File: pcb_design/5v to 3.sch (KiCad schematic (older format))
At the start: 6 parts

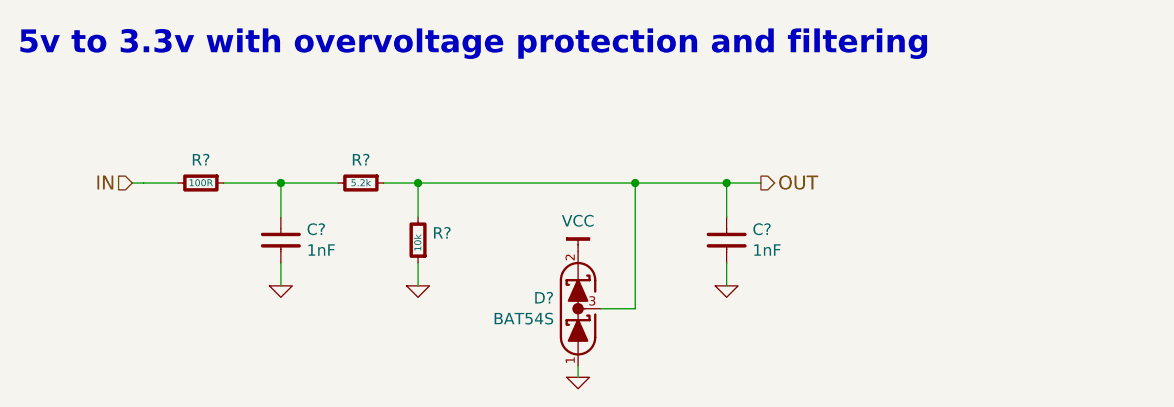
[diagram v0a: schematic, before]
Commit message: Components placement, 3D models, updated some footprints to nominal IPC type
Signed-off-by: Marcos Chaparro <mchaparro@paltatech.com>
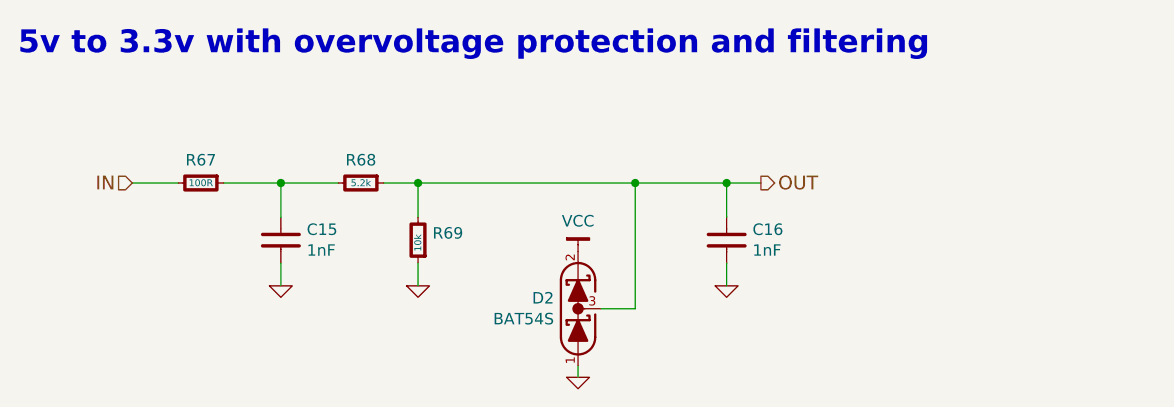
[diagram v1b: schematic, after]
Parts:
- gave numbers to parts that had none: 6
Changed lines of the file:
@@
 $Descr A4 11693 8268
 encoding utf-8
-Sheet 12 12
+Sheet 11 12
 Title ""
 Date ""
@@
 OUT
 $Comp
-L BAT54S D?
+L BAT54S D1
 U 1 1 5889F39B
 P 5950 4300
-AR Path="/5889B2E2/5889F39B" Ref="D?"  Part="1"
-AR Path="/5889CDF9/5889F39B" Ref="D?"  Part="1"
-F 0 "D?" V 5996 4195 50  0000 R CNN
+AR Path="/5889B2E2/5889F39B" Ref="D1"  Part="1"
+AR Path="/5889CDF9/5889F39B" Ref="D2"  Part="1"
+F 0 "D2" V 5996 4195 50  0000 R CNN
 F 1 "BAT54S" V 5905 4195 50  0000 R CNN
 F 2 "smd-semi:SOT-23" H 5950 4150 60  0001 C CNN
@@
 $EndComp
 $Comp
-L GND #PWR?
+L GND #PWR91
 U 1 1 5889F466
 P 5950 4600
-AR Path="/5889B2E2/5889F466" Ref="#PWR?"  Part="1"
-AR Path="/5889CDF9/5889F466" Ref="#PWR?"  Part="1"
-F 0 "#PWR?" H 5950 4600 30  0001 C CNN
+AR Path="/5889B2E2/5889F466" Ref="#PWR91"  Part="1"
+AR Path="/5889CDF9/5889F466" Ref="#PWR96"  Part="1"
+F 0 "#PWR96" H 5950 4600 30  0001 C CNN
 F 1 "GND" H 5950 4530 30  0001 C CNN
 F 2 "" H 5950 4600 60  0000 C CNN
@@
 $EndComp
 $Comp
-L R-0603 R?
+L R-0603 R64
 U 1 1 5889F74D
 P 4300 3750
-AR Path="/5889B2E2/5889F74D" Ref="R?"  Part="1"
-AR Path="/5889CDF9/5889F74D" Ref="R?"  Part="1"
-F 0 "R?" V 4200 3750 50  0000 C CNN
+AR Path="/5889B2E2/5889F74D" Ref="R64"  Part="1"
+AR Path="/5889CDF9/5889F74D" Ref="R67"  Part="1"
+F 0 "R67" V 4200 3750 50  0000 C CNN
 F 1 "100R" V 4300 3750 30  0000 C CNN
 F 2 "IPC7351-Nominal:RESC1608X50" H 4300 3750 50  0001 C CNN
@@
 $EndComp
 $Comp
-L R-0603 R?
+L R-0603 R65
 U 1 1 5889F796
 P 5000 3750
-AR Path="/5889B2E2/5889F796" Ref="R?"  Part="1"
-AR Path="/5889CDF9/5889F796" Ref="R?"  Part="1"
-F 0 "R?" V 4900 3750 50  0000 C CNN
+AR Path="/5889B2E2/5889F796" Ref="R65"  Part="1"
+AR Path="/5889CDF9/5889F796" Ref="R68"  Part="1"
+F 0 "R68" V 4900 3750 50  0000 C CNN
 F 1 "5.2k" V 5000 3750 30  0000 C CNN
 F 2 "IPC7351-Nominal:RESC1608X50" H 5000 3750 50  0001 C CNN
@@
 $EndComp
 $Comp
-L R-0603 R?
+L R-0603 R66
 U 1 1 5889F7E7
 P 5250 4000
-AR Path="/5889B2E2/5889F7E7" Ref="R?"  Part="1"
-AR Path="/5889CDF9/5889F7E7" Ref="R?"  Part="1"
-F 0 "R?" H 5187 3970 50  0000 R CNN
+AR Path="/5889B2E2/5889F7E7" Ref="R66"  Part="1"
+AR Path="/5889CDF9/5889F7E7" Ref="R69"  Part="1"
+F 0 "R69" H 5187 3970 50  0000 R CNN
 F 1 "10k" V 5250 4050 30  0000 R CNN
 F 2 "IPC7351-Nominal:RESC1608X50" H 5250 4000 50  0001 C CNN
@@
 $EndComp
 $Comp
-L C-0603 C?
+L C-0603 C13
 U 1 1 5889F81D
 P 4650 4000
-AR Path="/5889B2E2/5889F81D" Ref="C?"  Part="1"
-AR Path="/5889CDF9/5889F81D" Ref="C?"  Part="1"
-F 0 "C?" H 4763 4046 50  0000 L CNN
+AR Path="/5889B2E2/5889F81D" Ref="C13"  Part="1"
+AR Path="/5889CDF9/5889F81D" Ref="C15"  Part="1"
+F 0 "C15" H 4763 4046 50  0000 L CNN
 F 1 "1nF" H 4763 3955 50  0000 L CNN
 F 2 "IPC7351-Nominal:CAPC1608X55" H 4650 4000 50  0001 C CNN
@@
 $EndComp
 $Comp
-L GND #PWR?
+L GND #PWR89
 U 1 1 5889F89D
 P 5250 4200
-AR Path="/5889B2E2/5889F89D" Ref="#PWR?"  Part="1"
-AR Path="/5889CDF9/5889F89D" Ref="#PWR?"  Part="1"
-F 0 "#PWR?" H 5250 4200 30  0001 C CNN
+AR Path="/5889B2E2/5889F89D" Ref="#PWR89"  Part="1"
+AR Path="/5889CDF9/5889F89D" Ref="#PWR94"  Part="1"
+F 0 "#PWR94" H 5250 4200 30  0001 C CNN
 F 1 "GND" H 5250 4130 30  0001 C CNN
 F 2 "" H 5250 4200 60  0000 C CNN
@@
 $EndComp
 $Comp
-L GND #PWR?
+L GND #PWR88
 U 1 1 5889F8B7
 P 4650 4200
-AR Path="/5889B2E2/5889F8B7" Ref="#PWR?"  Part="1"
-AR Path="/5889CDF9/5889F8B7" Ref="#PWR?"  Part="1"
-F 0 "#PWR?" H 4650 4200 30  0001 C CNN
+AR Path="/5889B2E2/5889F8B7" Ref="#PWR88"  Part="1"
+AR Path="/5889CDF9/5889F8B7" Ref="#PWR93"  Part="1"
+F 0 "#PWR93" H 4650 4200 30  0001 C CNN
 F 1 "GND" H 4650 4130 30  0001 C CNN
 F 2 "" H 4650 4200 60  0000 C CNN
@@
 $EndComp
 $Comp
-L VCC #PWR?
+L VCC #PWR90
 U 1 1 5889F92D
 P 5950 4050
-AR Path="/5889B2E2/5889F92D" Ref="#PWR?"  Part="1"
-AR Path="/5889CDF9/5889F92D" Ref="#PWR?"  Part="1"
-F 0 "#PWR?" H 5950 4100 30  0001 C CNN
+AR Path="/5889B2E2/5889F92D" Ref="#PWR90"  Part="1"
+AR Path="/5889CDF9/5889F92D" Ref="#PWR95"  Part="1"
+F 0 "#PWR95" H 5950 4100 30  0001 C CNN
 F 1 "VCC" H 5950 4183 50  0000 C CNN
 F 2 "" H 5950 4050 60  0000 C CNN
@@
 $EndComp
 $Comp
-L C-0603 C?
+L C-0603 C14
 U 1 1 5889FB1A
 P 6600 4000
-AR Path="/5889B2E2/5889FB1A" Ref="C?"  Part="1"
-AR Path="/5889CDF9/5889FB1A" Ref="C?"  Part="1"
-F 0 "C?" H 6713 4046 50  0000 L CNN
+AR Path="/5889B2E2/5889FB1A" Ref="C14"  Part="1"
+AR Path="/5889CDF9/5889FB1A" Ref="C16"  Part="1"
+F 0 "C16" H 6713 4046 50  0000 L CNN
 F 1 "1nF" H 6713 3955 50  0000 L CNN
 F 2 "IPC7351-Nominal:CAPC1608X55" H 6600 4000 50  0001 C CNN
@@
 $EndComp
 $Comp
-L GND #PWR?
+L GND #PWR92
 U 1 1 5889FBDC
 P 6600 4200
-AR Path="/5889B2E2/5889FBDC" Ref="#PWR?"  Part="1"
-AR Path="/5889CDF9/5889FBDC" Ref="#PWR?"  Part="1"
-F 0 "#PWR?" H 6600 4200 30  0001 C CNN
+AR Path="/5889B2E2/5889FBDC" Ref="#PWR92"  Part="1"
+AR Path="/5889CDF9/5889FBDC" Ref="#PWR97"  Part="1"
+F 0 "#PWR97" H 6600 4200 30  0001 C CNN
 F 1 "GND" H 6600 4130 30  0001 C CNN
 F 2 "" H 6600 4200 60  0000 C CNN
@@
 	6200 4300 6200 3750
 Wire Wire Line
-	5100 3750 5250 3750
-Wire Wire Line
-	5250 3750 6200 3750
-Wire Wire Line
-	6200 3750 6600 3750
-Wire Wire Line
-	6600 3750 6750 3750
+	5100 3750 6750 3750
 Wire Wire Line
 	5950 4550 5950 4600
 Wire Wire Line
-	4200 3750 4050 3750
-Wire Wire Line
-	4050 3750 4000 3750
+	4000 3750 4200 3750
 Wire Wire Line
 	4650 3900 4650 3750
 Wire Wire Line
-	4400 3750 4650 3750
-Wire Wire Line
-	4650 3750 4900 3750
+	4400 3750 4900 3750
 Connection ~ 4650 3750
 Wire Wire Line

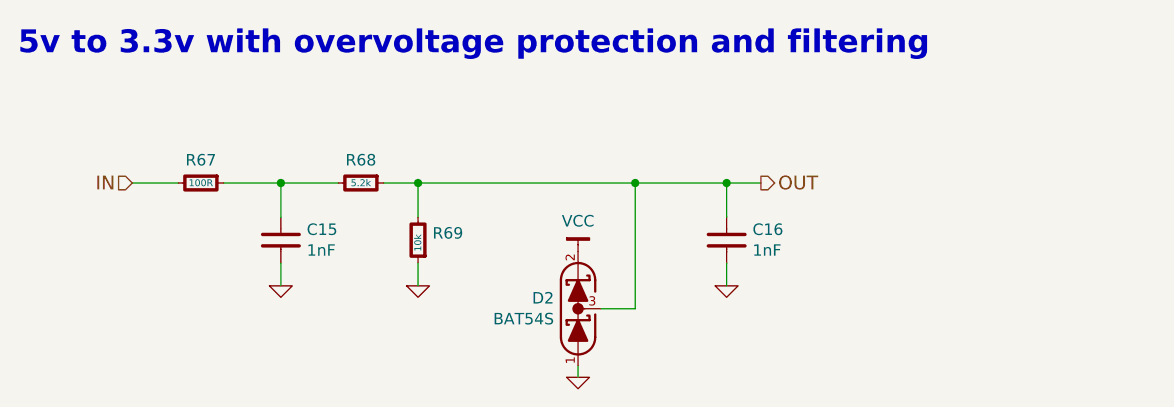
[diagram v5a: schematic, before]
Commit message: More layout. Changed LED pin. Added placeholder for a resolver IC
Signed-off-by: Marcos Chaparro <mchaparro@paltatech.com>
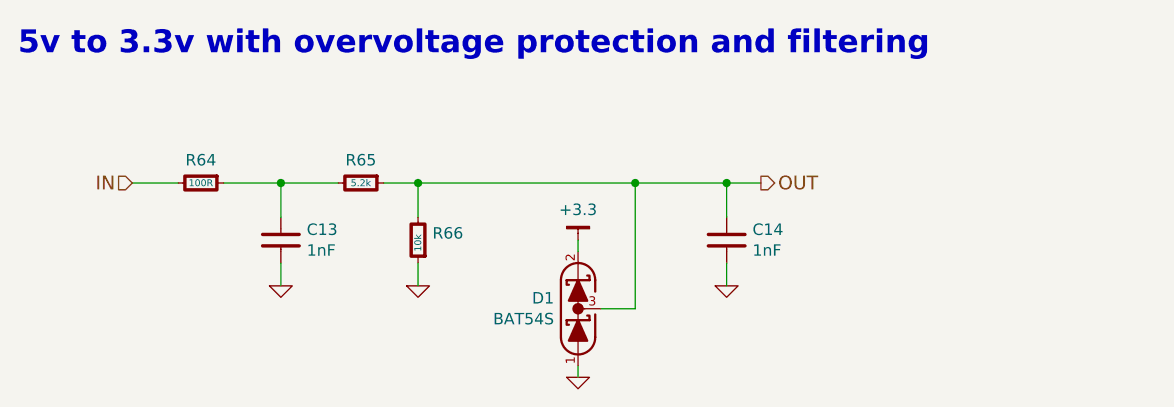
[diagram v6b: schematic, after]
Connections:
- net VCC renamed +3.3
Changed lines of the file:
@@
 $Descr A4 11693 8268
 encoding utf-8
-Sheet 11 13
+Sheet 11 14
 Title "5v to 3.3v conditioning"
 Date "2017-01-24"
@@
 AR Path="/5889B2E2/5889F39B" Ref="D1"  Part="1"
 AR Path="/5889CDF9/5889F39B" Ref="D2"  Part="1"
-F 0 "D2" V 5996 4195 50  0000 R CNN
+F 0 "D1" V 5996 4195 50  0000 R CNN
 F 1 "BAT54S" V 5905 4195 50  0000 R CNN
 F 2 "smd-semi:SOT-23" H 5950 4150 60  0001 C CNN
@@
 $EndComp
 $Comp
-L GND #PWR138
+L GND #PWR0135
 U 1 1 5889F466
 P 5950 4600
-AR Path="/5889B2E2/5889F466" Ref="#PWR138"  Part="1"
-AR Path="/5889CDF9/5889F466" Ref="#PWR143"  Part="1"
-F 0 "#PWR143" H 5950 4600 30  0001 C CNN
+AR Path="/5889B2E2/5889F466" Ref="#PWR0135"  Part="1"
+AR Path="/5889CDF9/5889F466" Ref="#PWR0140"  Part="1"
+F 0 "#PWR0135" H 5950 4600 30  0001 C CNN
 F 1 "GND" H 5950 4530 30  0001 C CNN
 F 2 "" H 5950 4600 60  0000 C CNN
@@
 AR Path="/5889B2E2/5889F74D" Ref="R64"  Part="1"
 AR Path="/5889CDF9/5889F74D" Ref="R67"  Part="1"
-F 0 "R67" V 4200 3750 50  0000 C CNN
+F 0 "R64" V 4200 3750 50  0000 C CNN
 F 1 "100R" V 4300 3750 30  0000 C CNN
 F 2 "IPC7351-Nominal:RESC1608X50" H 4300 3750 50  0001 C CNN
@@
 AR Path="/5889B2E2/5889F796" Ref="R65"  Part="1"
 AR Path="/5889CDF9/5889F796" Ref="R68"  Part="1"
-F 0 "R68" V 4900 3750 50  0000 C CNN
+F 0 "R65" V 4900 3750 50  0000 C CNN
 F 1 "5.2k" V 5000 3750 30  0000 C CNN
 F 2 "IPC7351-Nominal:RESC1608X50" H 5000 3750 50  0001 C CNN
@@
 AR Path="/5889B2E2/5889F7E7" Ref="R66"  Part="1"
 AR Path="/5889CDF9/5889F7E7" Ref="R69"  Part="1"
-F 0 "R69" H 5187 3970 50  0000 R CNN
+F 0 "R66" H 5187 3970 50  0000 R CNN
 F 1 "10k" V 5250 4050 30  0000 R CNN
 F 2 "IPC7351-Nominal:RESC1608X50" H 5250 4000 50  0001 C CNN
@@
 AR Path="/5889B2E2/5889F81D" Ref="C13"  Part="1"
 AR Path="/5889CDF9/5889F81D" Ref="C15"  Part="1"
-F 0 "C15" H 4763 4046 50  0000 L CNN
+F 0 "C13" H 4763 4046 50  0000 L CNN
 F 1 "1nF" H 4763 3955 50  0000 L CNN
 F 2 "IPC7351-Nominal:CAPC1608X55" H 4650 4000 50  0001 C CNN
@@
 $EndComp
 $Comp
-L GND #PWR136
+L GND #PWR0136
 U 1 1 5889F89D
 P 5250 4200
-AR Path="/5889B2E2/5889F89D" Ref="#PWR136"  Part="1"
-AR Path="/5889CDF9/5889F89D" Ref="#PWR141"  Part="1"
-F 0 "#PWR141" H 5250 4200 30  0001 C CNN
+AR Path="/5889B2E2/5889F89D" Ref="#PWR0136"  Part="1"
+AR Path="/5889CDF9/5889F89D" Ref="#PWR0141"  Part="1"
+F 0 "#PWR0136" H 5250 4200 30  0001 C CNN
 F 1 "GND" H 5250 4130 30  0001 C CNN
 F 2 "" H 5250 4200 60  0000 C CNN
@@
 $EndComp
 $Comp
-L GND #PWR135
+L GND #PWR0137
 U 1 1 5889F8B7
 P 4650 4200
-AR Path="/5889B2E2/5889F8B7" Ref="#PWR135"  Part="1"
-AR Path="/5889CDF9/5889F8B7" Ref="#PWR140"  Part="1"
-F 0 "#PWR140" H 4650 4200 30  0001 C CNN
+AR Path="/5889B2E2/5889F8B7" Ref="#PWR0137"  Part="1"
+AR Path="/5889CDF9/5889F8B7" Ref="#PWR0142"  Part="1"
+F 0 "#PWR0137" H 4650 4200 30  0001 C CNN
 F 1 "GND" H 4650 4130 30  0001 C CNN
 F 2 "" H 4650 4200 60  0000 C CNN
 F 3 "" H 4650 4200 60  0000 C CNN
 	1    4650 4200
-	1    0    0    -1
-$EndComp
-$Comp
-L VCC #PWR137
-U 1 1 5889F92D
-P 5950 4050
-AR Path="/5889B2E2/5889F92D" Ref="#PWR137"  Part="1"
-AR Path="/5889CDF9/5889F92D" Ref="#PWR142"  Part="1"
-F 0 "#PWR142" H 5950 4100 30  0001 C CNN
-F 1 "VCC" H 5950 4183 50  0000 C CNN
-F 2 "" H 5950 4050 60  0000 C CNN
-F 3 "" H 5950 4050 60  0000 C CNN
-	1    5950 4050
 	1    0    0    -1
 $EndComp
@@
 AR Path="/5889B2E2/5889FB1A" Ref="C14"  Part="1"
 AR Path="/5889CDF9/5889FB1A" Ref="C16"  Part="1"
-F 0 "C16" H 6713 4046 50  0000 L CNN
+F 0 "C14" H 6713 4046 50  0000 L CNN
 F 1 "1nF" H 6713 3955 50  0000 L CNN
 F 2 "IPC7351-Nominal:CAPC1608X55" H 6600 4000 50  0001 C CNN
@@
 $EndComp
 $Comp
-L GND #PWR139
+L GND #PWR0139
 U 1 1 5889FBDC
 P 6600 4200
-AR Path="/5889B2E2/5889FBDC" Ref="#PWR139"  Part="1"
-AR Path="/5889CDF9/5889FBDC" Ref="#PWR144"  Part="1"
-F 0 "#PWR144" H 6600 4200 30  0001 C CNN
+AR Path="/5889B2E2/5889FBDC" Ref="#PWR0139"  Part="1"
+AR Path="/5889CDF9/5889FBDC" Ref="#PWR0144"  Part="1"
+F 0 "#PWR0139" H 6600 4200 30  0001 C CNN
 F 1 "GND" H 6600 4130 30  0001 C CNN
 F 2 "" H 6600 4200 60  0000 C CNN
@@
 Text Notes 3500 3200 0    100  ~ 20
 5v to 3.3v with overvoltage protection and filtering
+$Comp
+L +3.3 #PWR?
+U 1 1 588FFFB4
+P 5950 4000
+F 0 "#PWR?" H 0   50  30  0001 C CNN
+F 1 "+3.3" H 5950 4133 50  0000 C CNN
+F 2 "" H 0   0   60  0000 C CNN
+F 3 "" H 0   0   60  0000 C CNN
+	1    5950 4000
+	1    0    0    -1
+$EndComp
+Wire Wire Line
+	5950 4000 5950 4050
 $EndSCHEMATC

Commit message: Added reverse polarity protection on the isolated side of CON connector. Also, more layout
Signed-off-by: Marcos Chaparro <mchaparro@paltatech.com>
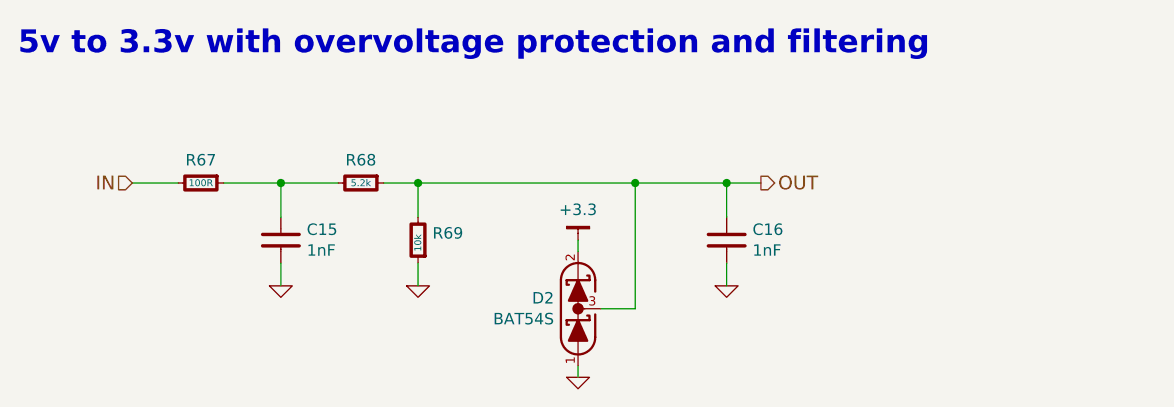
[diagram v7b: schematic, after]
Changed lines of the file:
@@
 AR Path="/5889B2E2/5889F39B" Ref="D1"  Part="1"
 AR Path="/5889CDF9/5889F39B" Ref="D2"  Part="1"
-F 0 "D1" V 5996 4195 50  0000 R CNN
+F 0 "D2" V 5996 4195 50  0000 R CNN
 F 1 "BAT54S" V 5905 4195 50  0000 R CNN
 F 2 "smd-semi:SOT-23" H 5950 4150 60  0001 C CNN
@@
 $EndComp
 $Comp
-L GND #PWR0135
+L GND #PWR142
 U 1 1 5889F466
 P 5950 4600
-AR Path="/5889B2E2/5889F466" Ref="#PWR0135"  Part="1"
-AR Path="/5889CDF9/5889F466" Ref="#PWR0140"  Part="1"
-F 0 "#PWR0135" H 5950 4600 30  0001 C CNN
+AR Path="/5889B2E2/5889F466" Ref="#PWR142"  Part="1"
+AR Path="/5889CDF9/5889F466" Ref="#PWR147"  Part="1"
+F 0 "#PWR147" H 5950 4600 30  0001 C CNN
 F 1 "GND" H 5950 4530 30  0001 C CNN
 F 2 "" H 5950 4600 60  0000 C CNN
@@
 AR Path="/5889B2E2/5889F74D" Ref="R64"  Part="1"
 AR Path="/5889CDF9/5889F74D" Ref="R67"  Part="1"
-F 0 "R64" V 4200 3750 50  0000 C CNN
+F 0 "R67" V 4200 3750 50  0000 C CNN
 F 1 "100R" V 4300 3750 30  0000 C CNN
 F 2 "IPC7351-Nominal:RESC1608X50" H 4300 3750 50  0001 C CNN
@@
 AR Path="/5889B2E2/5889F796" Ref="R65"  Part="1"
 AR Path="/5889CDF9/5889F796" Ref="R68"  Part="1"
-F 0 "R65" V 4900 3750 50  0000 C CNN
+F 0 "R68" V 4900 3750 50  0000 C CNN
 F 1 "5.2k" V 5000 3750 30  0000 C CNN
 F 2 "IPC7351-Nominal:RESC1608X50" H 5000 3750 50  0001 C CNN
@@
 AR Path="/5889B2E2/5889F7E7" Ref="R66"  Part="1"
 AR Path="/5889CDF9/5889F7E7" Ref="R69"  Part="1"
-F 0 "R66" H 5187 3970 50  0000 R CNN
+F 0 "R69" H 5187 3970 50  0000 R CNN
 F 1 "10k" V 5250 4050 30  0000 R CNN
 F 2 "IPC7351-Nominal:RESC1608X50" H 5250 4000 50  0001 C CNN
@@
 AR Path="/5889B2E2/5889F81D" Ref="C13"  Part="1"
 AR Path="/5889CDF9/5889F81D" Ref="C15"  Part="1"
-F 0 "C13" H 4763 4046 50  0000 L CNN
+F 0 "C15" H 4763 4046 50  0000 L CNN
 F 1 "1nF" H 4763 3955 50  0000 L CNN
 F 2 "IPC7351-Nominal:CAPC1608X55" H 4650 4000 50  0001 C CNN
@@
 $EndComp
 $Comp
-L GND #PWR0136
+L GND #PWR140
 U 1 1 5889F89D
 P 5250 4200
-AR Path="/5889B2E2/5889F89D" Ref="#PWR0136"  Part="1"
-AR Path="/5889CDF9/5889F89D" Ref="#PWR0141"  Part="1"
-F 0 "#PWR0136" H 5250 4200 30  0001 C CNN
+AR Path="/5889B2E2/5889F89D" Ref="#PWR140"  Part="1"
+AR Path="/5889CDF9/5889F89D" Ref="#PWR145"  Part="1"
+F 0 "#PWR145" H 5250 4200 30  0001 C CNN
 F 1 "GND" H 5250 4130 30  0001 C CNN
 F 2 "" H 5250 4200 60  0000 C CNN
@@
 $EndComp
 $Comp
-L GND #PWR0137
+L GND #PWR139
 U 1 1 5889F8B7
 P 4650 4200
-AR Path="/5889B2E2/5889F8B7" Ref="#PWR0137"  Part="1"
-AR Path="/5889CDF9/5889F8B7" Ref="#PWR0142"  Part="1"
-F 0 "#PWR0137" H 4650 4200 30  0001 C CNN
+AR Path="/5889B2E2/5889F8B7" Ref="#PWR139"  Part="1"
+AR Path="/5889CDF9/5889F8B7" Ref="#PWR144"  Part="1"
+F 0 "#PWR144" H 4650 4200 30  0001 C CNN
 F 1 "GND" H 4650 4130 30  0001 C CNN
 F 2 "" H 4650 4200 60  0000 C CNN
@@
 AR Path="/5889B2E2/5889FB1A" Ref="C14"  Part="1"
 AR Path="/5889CDF9/5889FB1A" Ref="C16"  Part="1"
-F 0 "C14" H 6713 4046 50  0000 L CNN
+F 0 "C16" H 6713 4046 50  0000 L CNN
 F 1 "1nF" H 6713 3955 50  0000 L CNN
 F 2 "IPC7351-Nominal:CAPC1608X55" H 6600 4000 50  0001 C CNN
@@
 $EndComp
 $Comp
-L GND #PWR0139
+L GND #PWR143
 U 1 1 5889FBDC
 P 6600 4200
-AR Path="/5889B2E2/5889FBDC" Ref="#PWR0139"  Part="1"
-AR Path="/5889CDF9/5889FBDC" Ref="#PWR0144"  Part="1"
-F 0 "#PWR0139" H 6600 4200 30  0001 C CNN
+AR Path="/5889B2E2/5889FBDC" Ref="#PWR143"  Part="1"
+AR Path="/5889CDF9/5889FBDC" Ref="#PWR148"  Part="1"
+F 0 "#PWR148" H 6600 4200 30  0001 C CNN
 F 1 "GND" H 6600 4130 30  0001 C CNN
 F 2 "" H 6600 4200 60  0000 C CNN
@@
 5v to 3.3v with overvoltage protection and filtering
 $Comp
-L +3.3 #PWR?
+L +3.3 #PWR141
 U 1 1 588FFFB4
 P 5950 4000
-F 0 "#PWR?" H 0   50  30  0001 C CNN
+AR Path="/5889B2E2/588FFFB4" Ref="#PWR141"  Part="1"
+AR Path="/5889CDF9/588FFFB4" Ref="#PWR146"  Part="1"
+F 0 "#PWR146" H 0   50  30  0001 C CNN
 F 1 "+3.3" H 5950 4133 50  0000 C CNN
 F 2 "" H 0   0   60  0000 C CNN
